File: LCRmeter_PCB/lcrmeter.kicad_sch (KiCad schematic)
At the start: 70 parts, among them IC1 TPS2116DRLR, J1 LCR_input, J2 LCR_input, J3 Prog_interface, J4 USB_B_Micro, J6 misc, J7 misc, Q1 NX7002BKR, SW1 power, SW2 up, SW3 down, SW4 ok, SW5 back, U1 74LVC1G66, U10 MCP6001-OT, U2 74LVC1G66, U3 OLED, U4 74HC14, U5 LMH6645, U6 STM32G473C_B-C-E_Tx, U7 74LVC1G66, U8 LMH6645, U9 LM1117MP-3.3

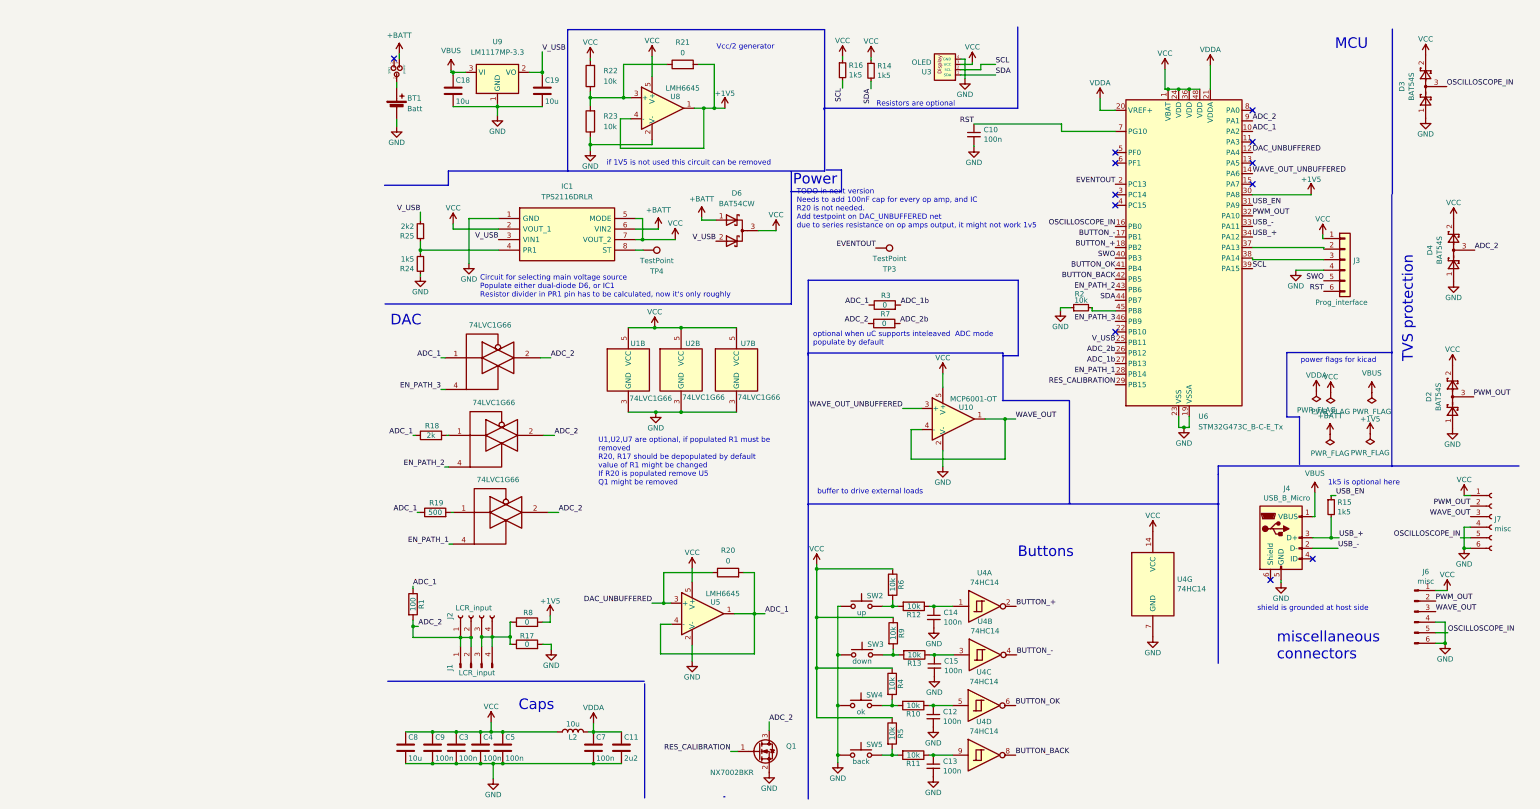
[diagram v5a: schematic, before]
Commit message: removed unnecessarry components
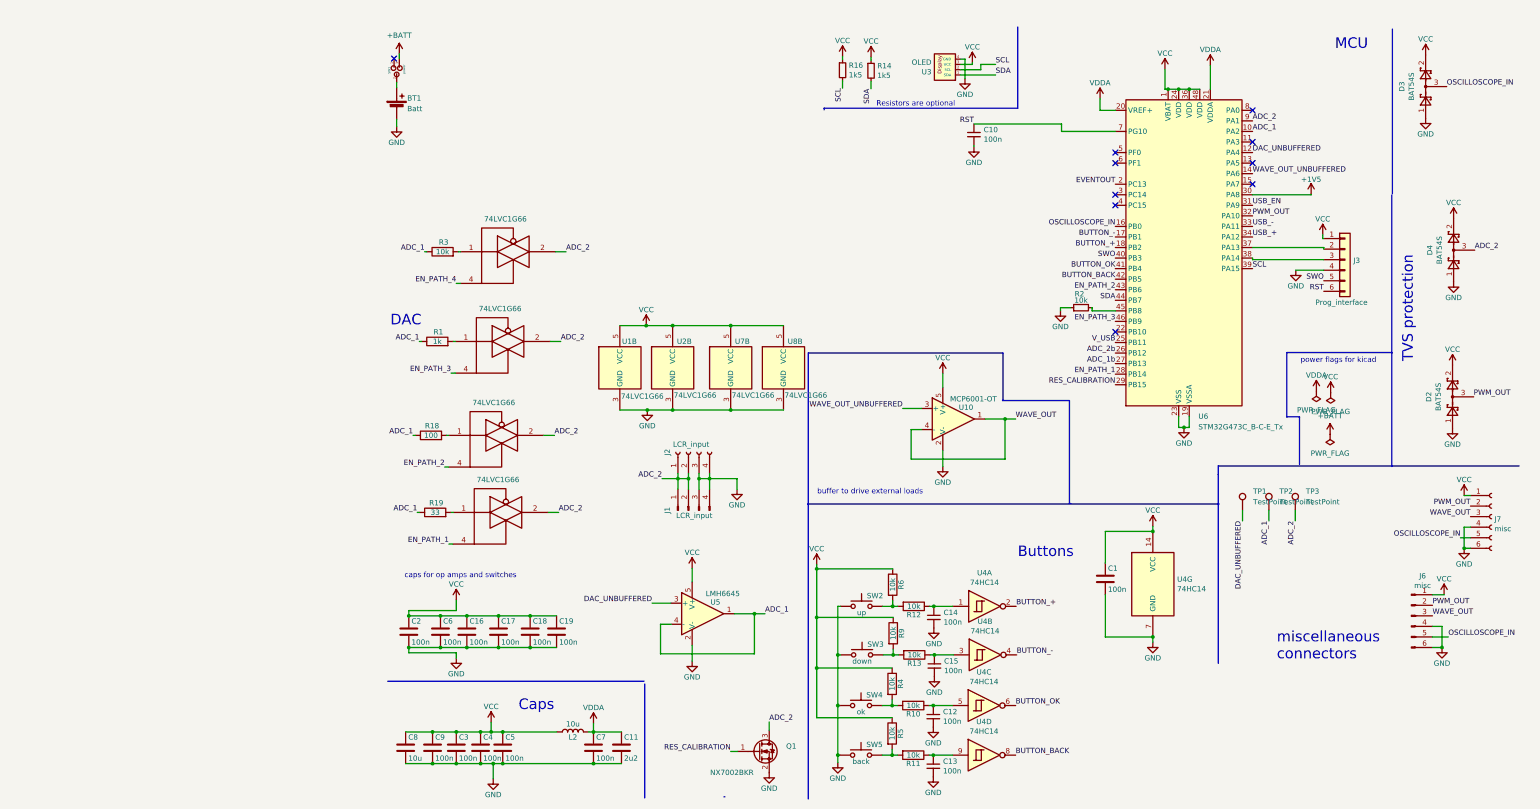
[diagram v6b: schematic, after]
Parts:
- removed D6: BAT54CW, Package_TO_SOT_SMD:SOT-23, symbol Device:D_Schottky_Dual_CommonCathode_AAK_Parallel
- removed IC1: TPS2116DRLR, Library_Loader:SOTFL50P160X60-8N, symbol library_loader:TPS2116DRLR
- removed J4: USB_B_Micro, Connector_USB:USB_Micro-B_Molex_47346-0001, symbol lcrmeter-rescue:USB_B_Micro-Connector
- removed R15, R24: 1k5, Resistor_SMD:R_0805_2012Metric_Pad1.20x1.40mm_HandSolder, symbol Device:R_Small
- removed R17, R20, R21, R7, R8: 0, Resistor_SMD:R_0805_2012Metric_Pad1.20x1.40mm_HandSolder, symbol Device:R
- removed R22, R23: 10k, Resistor_SMD:R_0805_2012Metric_Pad1.20x1.40mm_HandSolder, symbol Device:R
- removed R25: 2k2, Resistor_SMD:R_0805_2012Metric_Pad1.20x1.40mm_HandSolder, symbol Device:R_Small
- removed TP4: TestPoint, TestPoint:TestPoint_Pad_1.0x1.0mm, symbol Connector:TestPoint
- removed U8: LMH6645, Package_TO_SOT_SMD:SOT-23-5, symbol Amplifier_Operational:MCP6001-OT
- removed U9: LM1117MP-3.3, Package_TO_SOT_SMD:SOT-223-3_TabPin2, symbol Regulator_Linear:LM1117MP-3.3
- added C1, C16, C17, C2, C6: 100n, Capacitor_SMD:C_0603_1608Metric_Pad1.08x0.95mm_HandSolder, symbol Device:C
- added TP1, TP2: TestPoint, symbol Connector:TestPoint
- added U8: 74LVC1G66, Package_TO_SOT_SMD:SOT-23-5, symbol 74xGxx:74LVC1G66
- C18, C19: value 10u -> 100n; footprint Capacitor_SMD:C_0805_2012Metric_Pad1.18x1.45mm_HandSolder -> Capacitor_SMD:C_0603_1608Metric_Pad1.08x0.95mm_HandSolder
- R1: value 100 -> 1k
- R18: value 2k -> 100
- R19: value 500 -> 33
- R3: value 0 -> 10k
- TP3: footprint TestPoint:TestPoint_Pad_1.0x1.0mm -> (none)
- U5: value LMH6645 -> LMH6645
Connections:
- net VBUS is gone; now on net VCC: C18.1
- net ADC_1: now also TP2.1; no longer U7.1
- net ADC_1b: no longer R3.2
- net ADC_2: now also TP3.1, U8.2; no longer R1.2
- net DAC_UNBUFFERED: now also TP1.1
- net EVENTOUT: no longer TP3.1
- net GND: now also J1.3 (Pin_3), J1.4 (Pin_4), J2.3 (Pin_3), J2.4 (Pin_4), C1.2, C16.2, C17.2, C2.2, C6.2, U8.3 (GND)
- net VCC: now also C19.1, C1.1, C16.1, C17.1, C2.1, C6.1, U8.5 (VCC)
- net V_USB: no longer C19.1
- new net: R1.2, U7.1
- new net: R3.2, U8.1
- new net EN_PATH_4: U8.4
- no-connect marks 12 -> 10
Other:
- note added: "caps for op amps and switches"
- note removed: "1k5 is optional here"
- note removed: "Circuit for selecting main voltage source Populate either dual-diode D6, or IC1 Resistor divider in PR1 pin has to be calculated, now it's only roughly"
- note removed: "Power"
- note removed: "TODO in next version Needs to add 100nF cap for every op amp, and IC R20 is not needed. Add testpoint on DAC_UNBUFFERED net due to series resistance on op amps output, it might not work 1v5"
- note removed: "U1,U2,U7 are optional, if populated R1 must be removed R20, R17 should be depopulated by default value of R1 might be changed If R20 is populated remove U5 Q1 might be removed"
- note removed: "Vcc/2 generator"
- note removed: "if 1V5 is not used this circuit can be removed"
- note removed: "optional when uC supports inteleaved ADC mode populate by default"
- note removed: "shield is grounded at host side"
- moved on the sheet: J1, J2, J6, U1B, U2B, U7B

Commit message: tentiative update of schematic to include active filters and discrete OLED
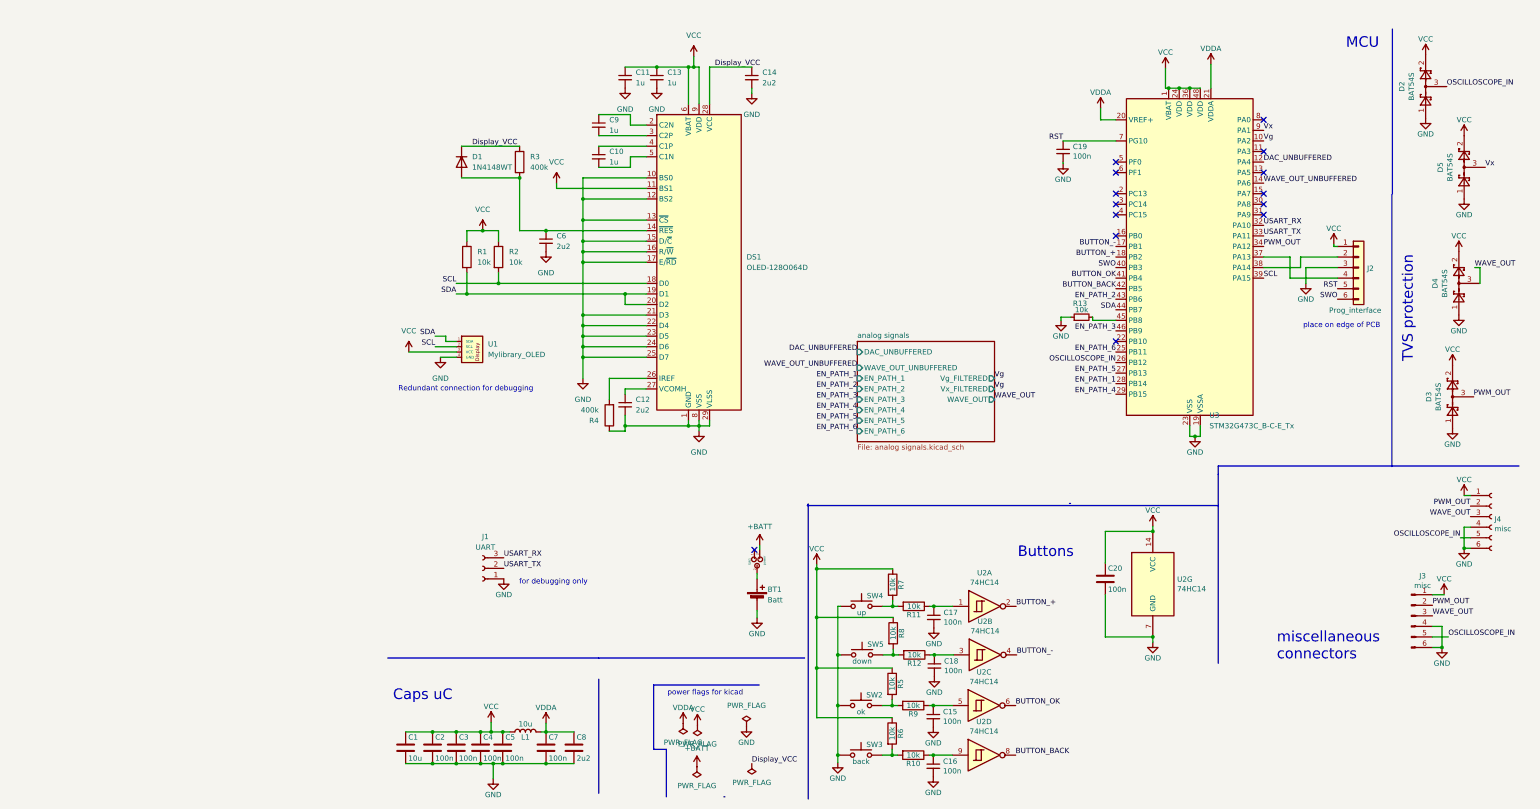
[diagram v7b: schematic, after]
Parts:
- removed C16, C17, C18, C19, C2, C6: 100n, Capacitor_SMD:C_0603_1608Metric_Pad1.08x0.95mm_HandSolder, symbol Device:C
- removed J1: LCR_input, Connector_PinHeader_2.54mm:PinHeader_1x04_P2.54mm_Vertical, symbol lcrmeter-rescue:Conn_01x04_Male
- removed J2: LCR_input, Connector_PinSocket_2.54mm:PinSocket_1x04_P2.54mm_Vertical, symbol lcrmeter-rescue:Conn_01x04_Female
- removed Q1: NX7002BKR, Package_TO_SOT_SMD:SOT-23, symbol Transistor_FET:2N7002
- removed R14, R16: 1k5, Resistor_SMD:R_0805_2012Metric_Pad1.20x1.40mm_HandSolder, symbol Device:R_Small
- removed R18: 100, Resistor_SMD:R_0805_2012Metric_Pad1.20x1.40mm_HandSolder, symbol Device:R
- removed R19: 33, Resistor_SMD:R_0805_2012Metric_Pad1.20x1.40mm_HandSolder, symbol Device:R
- removed TP1, TP2, TP3: TestPoint, symbol Connector:TestPoint
- removed U1, U2, U7, U8: 74LVC1G66, Package_TO_SOT_SMD:SOT-23-5, symbol 74xGxx:74LVC1G66
- removed U10: MCP6001-OT, Package_TO_SOT_SMD:SOT-23-5, symbol Amplifier_Operational:MCP6001-OT
- removed U3: OLED, footprints:OLED_128x64, symbol lcrmeter-rescue:OLED-Mylibrary
- removed U5: LMH6645, Package_TO_SOT_SMD:SOT-23-5, symbol Amplifier_Operational:MCP6001-OT
- added C10, C11, C13, C9: 1u, symbol Device:C_Small
- added C12, C14, C6: 2u2, symbol Device:C_Small
- added D1: 1N4148WT, Diode_SMD:D_SOD-523, symbol Diode:1N4148WT
- added D5: BAT54S, Package_TO_SOT_SMD:SOT-23, symbol lcrmeter-rescue:BAT54S-Diode
- added DS1: OLED-128O064D, Display:OLED-128O064D, symbol Display_Graphic:OLED-128O064D
- added J1: UART, symbol Connector:Conn_01x03_Socket
- added R2: 10k, symbol Device:R
- added R4: 400k, symbol Device:R
- added U1: Mylibrary_OLED, symbol lcrmeter-rescue:OLED-Mylibrary
- R1: value 1k -> 10k; footprint Resistor_SMD:R_0805_2012Metric_Pad1.20x1.40mm_HandSolder -> (none)
- R3: value 10k -> 400k; footprint Resistor_SMD:R_0805_2012Metric_Pad1.20x1.40mm_HandSolder -> (none)
- renumbered C8 to C1, C12 to C15, C13 to C16, C14 to C17, C15 to C18, C10 to C19, C9 to C2, C1 to C20, C11 to C8, D3 to D2, D2 to D3, J3 to J2, J6 to J3, J7 to J4, L2 to L1, R11 to R10, R12 to R11, R13 to R12, R2 to R13, R4 to R5, R5 to R6, R6 to R7, R9 to R8, R10 to R9, SW4 to SW2, SW5 to SW3, SW2 to SW4, SW3 to SW5, U4 to U2, U6 to U3
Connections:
- net ADC_2b is gone; now on net OSCILLOSCOPE_IN: U3.26 (PB12)
- net RES_CALIBRATION is gone; now on net EN_PATH_4: U3.29 (PB15)
- net USB_+ is gone; now on net PWM_OUT: U3.34 (PA12)
- net GND: now also J2.3 (Pin_3), C11.2, C12.2, C13.2, C14.2, C6.2, D5.1, DS1.1 (GND), DS1.10 (BS0), DS1.12 (BS2), DS1.13 (~{CS}), DS1.15 (D/~{C}), DS1.16 (R/~{W}), DS1.17 (E/~{RD}), DS1.21 (D3), DS1.22 (D4), DS1.23 (D5), DS1.24 (D6), DS1.25 (D7), DS1.29 (VLSS), DS1.30 (GND), DS1.8 (VSS), J1.1 (Pin_1), R4.1, U1.4 (GND); no longer J2.4 (Pin_4)
- net OSCILLOSCOPE_IN: no longer U3.16 (PB0)
- net PWM_OUT: no longer U3.32 (PA10)
- net RST: now also J2.5 (Pin_5); no longer J2.6 (Pin_6)
- net SCL: now also DS1.18 (D0), R2.2, U1.2 (SCL)
- net SDA: now also R1.2, DS1.19 (D1), DS1.20 (D2), U1.1 (SDA)
- net SWO: now also J2.6 (Pin_6); no longer J2.5 (Pin_5)
- net VCC: now also R1.1, C11.1, C13.1, D5.2, DS1.11 (BS1), DS1.6 (VBAT), DS1.9 (VDD), R2.1, U1.3 (VCC)
- net WAVE_OUT: now also D4.3
- net at J2.2 (Pin_2): now also U3.38 (PA14); no longer U3.37 (PA13)
- net at R3.2: now also C6.1, D1.2 (A), DS1.14 (~{RES})
- net +1V5: no longer names the net of U3.30 (PA8)
- removed net ADC_1: R1.1, R3.1, U3.10 (PA2)
- net ADC_1b renamed EN_PATH_5
- net ADC_2 renamed Vx
- net Vx: now also D5.3; no longer D4.3
- net EVENTOUT: no longer names the net of U3.2 (PC13)
- net USB_- renamed USART_TX
- net USART_TX: now also J1.2 (Pin_2)
- net USB_EN: no longer names the net of U3.31 (PA9)
- net V_USB renamed EN_PATH_6
- new net: J2.4 (Pin_4), U3.37 (PA13)
- new net: C9.1, DS1.2 (C2N)
- new net: DS1.26 (IREF), R4.2
- new net: C12.1, DS1.27 (VCOMH)
- new net: C9.2, DS1.3 (C2P)
- new net: C10.1, DS1.4 (C1P)
- new net: C10.2, DS1.5 (C1N)
- new net Display_VCC: C14.1, D1.1 (K), DS1.28 (VCC), R3.1
- new net USART_RX: J1.3 (Pin_3), U3.32 (PA10)
- new net Vg: U3.10 (PA2)
- no-connect marks 10 -> 14
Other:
- added sheet analog signals (analog signals.kicad_sch)
- note added: "Caps uC"
- note added: "Redundant connection for debugging"
- note added: "for debugging only"
- note added: "place on edge of PCB"
- note removed: "Caps"
- note removed: "DAC"
- note removed: "Resistors are optional"
- note removed: "buffer to drive external loads"
- note removed: "caps for op amps and switches"
- moved on the sheet: BT1, C19, C7, C8, D4, J2, L1, R13, SW1, U3

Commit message: Fix TG connection for Vg; component placement; filter basis
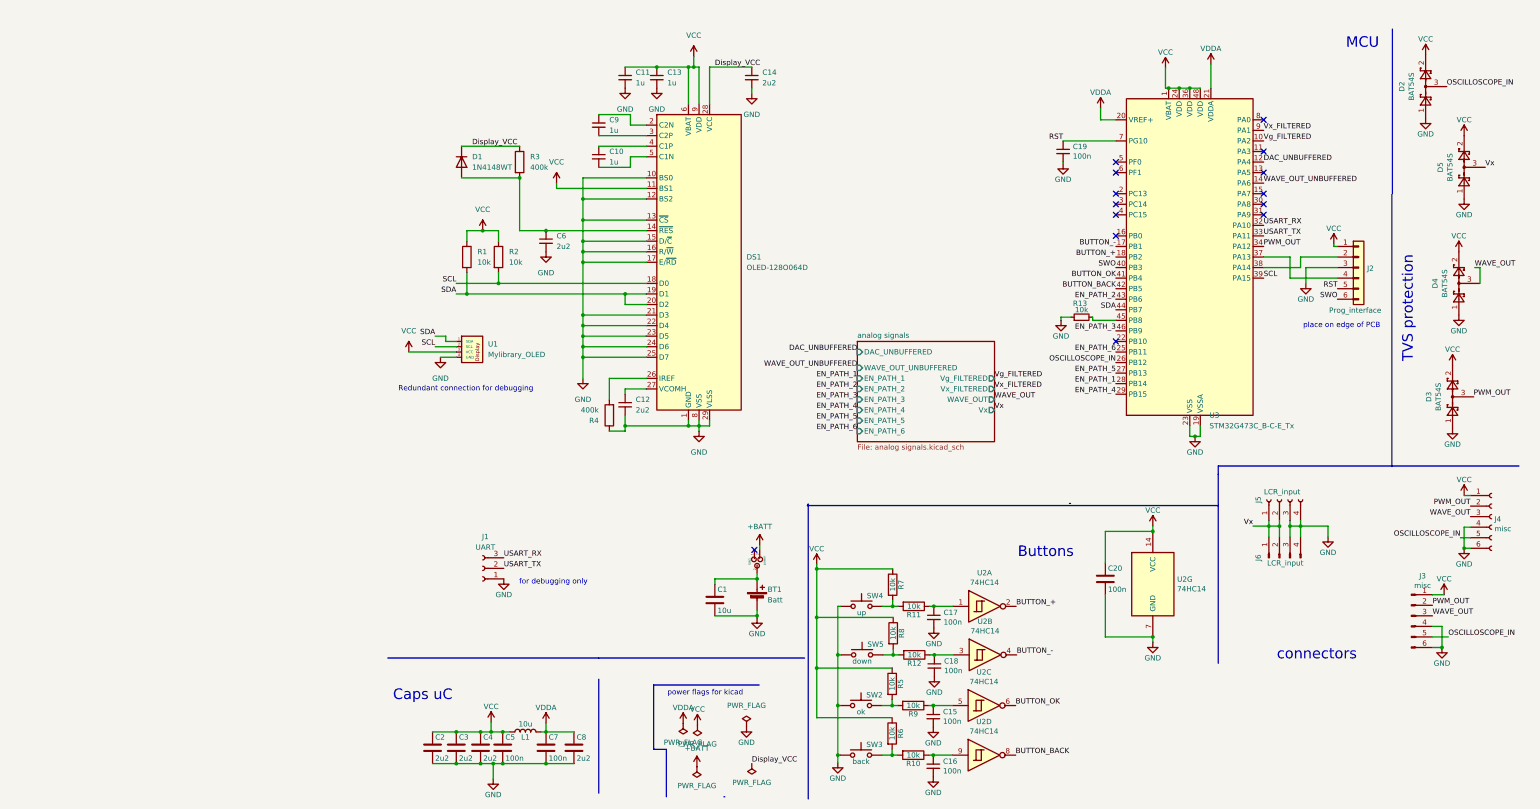
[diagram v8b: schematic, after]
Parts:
- added J5: LCR_input, Connector_PinSocket_2.54mm:PinSocket_1x04_P2.54mm_Vertical, symbol lcrmeter-rescue:Conn_01x04_Female
- added J6: LCR_input, Connector_PinHeader_2.54mm:PinHeader_1x04_P2.54mm_Vertical, symbol lcrmeter-rescue:Conn_01x04_Male
- C10, C11, C12, C13, C14, C6, C9: footprint (none) -> Capacitor_SMD:C_0402_1005Metric_Pad0.74x0.62mm_HandSolder
- C15, C16, C17, C18, C19, C20, C5, C7, C8: footprint Capacitor_SMD:C_0603_1608Metric_Pad1.08x0.95mm_HandSolder -> Capacitor_SMD:C_0402_1005Metric_Pad0.74x0.62mm_HandSolder
- C2, C3, C4: value 100n -> 2u2; footprint Capacitor_SMD:C_0603_1608Metric_Pad1.08x0.95mm_HandSolder -> Capacitor_SMD:C_0402_1005Metric_Pad0.74x0.62mm_HandSolder
- J1: footprint (none) -> Connector_Harwin:Harwin_M20-89003xx_1x03_P2.54mm_Horizontal
- J2: footprint Connector_PinHeader_2.54mm:PinHeader_1x06_P2.54mm_Vertical -> Connector_Harwin:Harwin_M20-89006xx_1x06_P2.54mm_Horizontal
- R1, R2, R3, R4: footprint (none) -> Resistor_SMD:R_0603_1608Metric_Pad0.98x0.95mm_HandSolder
- U1: footprint (none) -> Connector_PinHeader_2.54mm:PinHeader_1x04_P2.54mm_Vertical
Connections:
- net GND: now also J5.3 (Pin_3), J5.4 (Pin_4), J6.3 (Pin_3), J6.4 (Pin_4)
- net VCC: no longer C1.1
- net Vx: now also J5.1 (Pin_1), J5.2 (Pin_2), J6.1 (Pin_1), J6.2 (Pin_2); no longer U3.9 (PA1)
- net at BT1.1 (+), SW1.2: now also C1.1
- net Vg renamed Vg_FILTERED
- new net Vx_FILTERED: U3.9 (PA1)
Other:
- sheet analog signals ports: added Vx; removed none
- note added: "connectors"
- note removed: "miscellaneous connectors"
- moved on the sheet: C1
